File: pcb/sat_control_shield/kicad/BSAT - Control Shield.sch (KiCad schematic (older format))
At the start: 12 parts, among them P1 POWER, U1 ARDUINO_NANO_V3.0, U2 74HC4052E

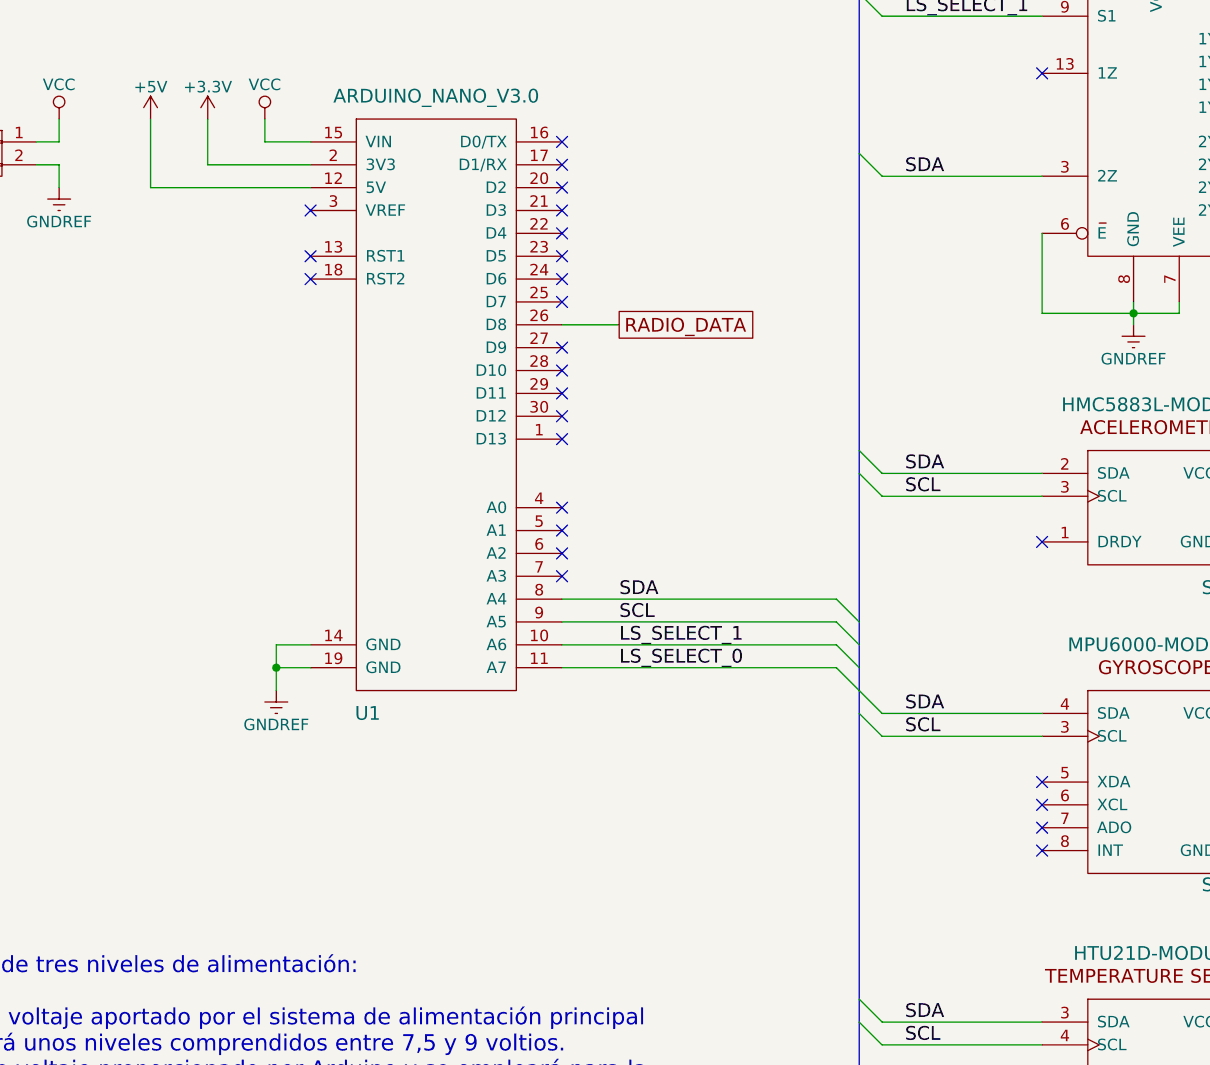
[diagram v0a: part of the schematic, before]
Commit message: refactor(control-shield): Rediseño de la placa y corrección de error en la conmutación entre sensores de intensidad luminosa.
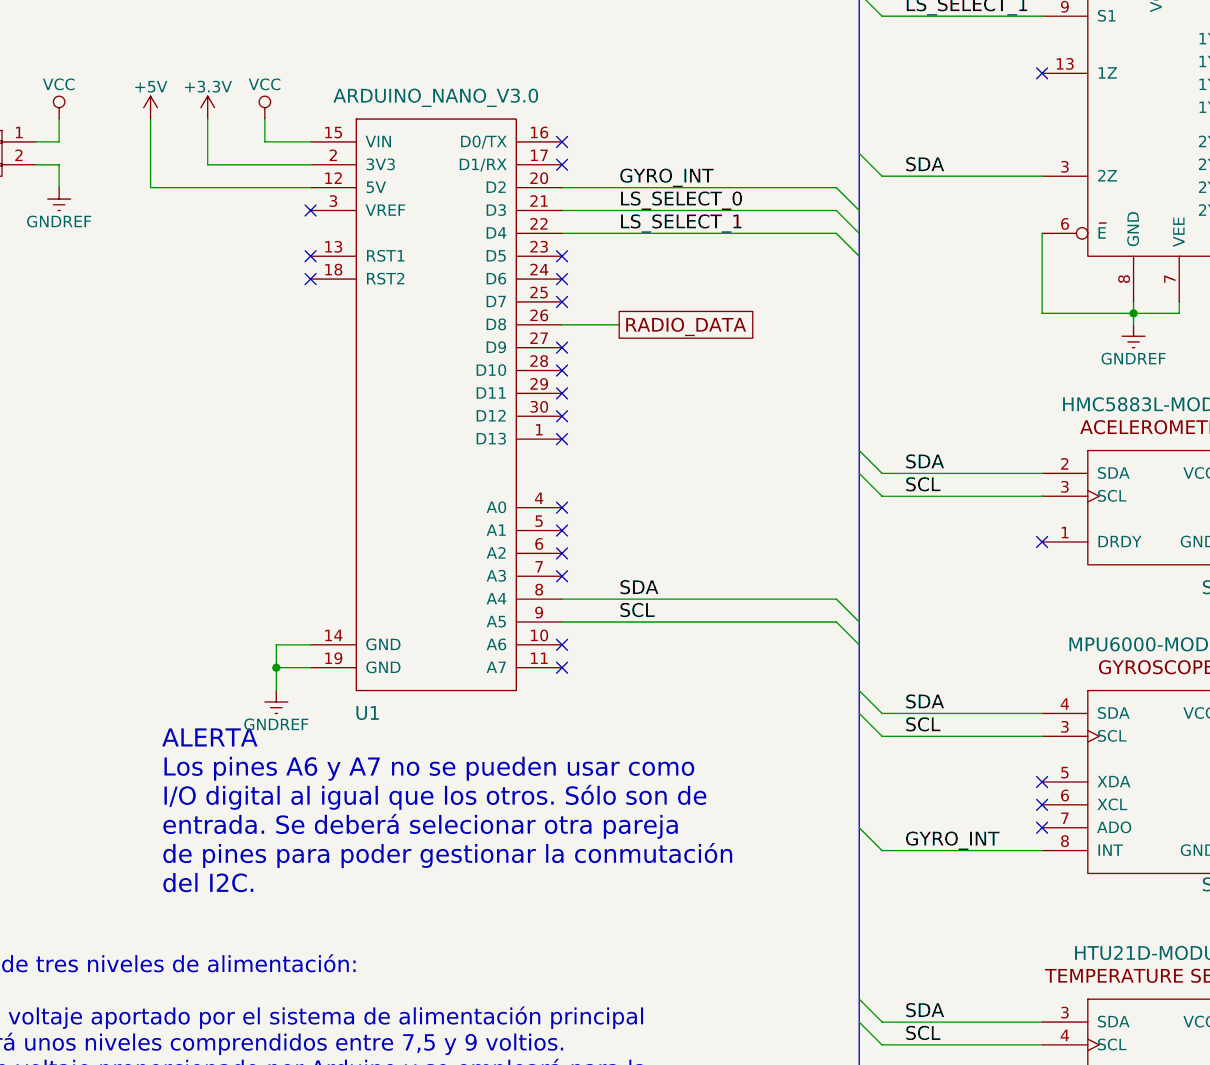
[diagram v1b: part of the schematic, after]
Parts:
- ANT1: footprint Pin_Headers:Pin_Header_Angled_1x01 -> Pin_Headers:Pin_Header_Angled_1x01_Pitch2.54mm
- P1: footprint Pin_Headers:Pin_Header_Straight_1x02 -> Pin_Headers:Pin_Header_Straight_1x02_Pitch2.54mm
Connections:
- net LS_SELECT_0: now also U1.21 (D3); no longer U1.11 (A7)
- net LS_SELECT_1: now also U1.22 (D4); no longer U1.10 (A6)
- net GYRO_INT: now reaches U1.20 (D2)
- net GYRO_INT: now also S2.8 (INT)
- no-connect marks 30 -> 28
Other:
- note added: "ALERTA\nLos pines A6 y A7 no se pueden usar como \nI/O digital al igual que los otros. Sólo son de \nentrada. Se deberá selecionar otra pareja \nde pines para poder gestionar la conmutación \ndel I2C."
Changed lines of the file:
@@
 F 0 "ANT1" H 8600 4850 60  0000 R CNN
 F 1 "ANTENNA-1" H 8600 4950 60  0000 R CNN
-F 2 "Pin_Headers:Pin_Header_Angled_1x01" H 8650 5000 60  0001 C CNN
+F 2 "Pin_Headers:Pin_Header_Angled_1x01_Pitch2.54mm" H 8650 5000 60  0001 C CNN
 F 3 "" H 8650 5000 60  0000 C CNN
 	1    8650 5000
@@
 F 0 "P1" H 1600 2300 50  0000 C CNN
 F 1 "POWER" V 1700 2150 50  0000 C CNN
-F 2 "Pin_Headers:Pin_Header_Straight_1x02" H 1600 2150 50  0001 C CNN
+F 2 "Pin_Headers:Pin_Header_Straight_1x02_Pitch2.54mm" H 1600 2150 50  0001 C CNN
 F 3 "" H 1600 2150 50  0000 C CNN
 	1    1600 2150
@@
 NoConn ~ 6200 5000
 NoConn ~ 6200 5100
-NoConn ~ 6200 5200
 $Comp
 L GNDREF #PWR017
@@
 Entry Wire Line
 	5300 4200 5400 4300
-Text Label 4350 4400 0    60   ~ 0
+Text Label 4350 2400 0    60   ~ 0
 LS_SELECT_0
-Text Label 4350 4300 0    60   ~ 0
+Text Label 4350 2500 0    60   ~ 0
 LS_SELECT_1
 Text Label 5600 1550 0    60   ~ 0
@@
 NoConn ~ 4100 2700
 NoConn ~ 4100 2600
-NoConn ~ 4100 2500
 NoConn ~ 4100 2200
 NoConn ~ 4100 2100
 NoConn ~ 4100 3200
 NoConn ~ 4100 3300
-NoConn ~ 4100 2300
-NoConn ~ 4100 2400
 Wire Wire Line
 	2800 2000 2800 2100
@@
 	5400 700  8100 700
 Entry Wire Line
-	5300 4300 5400 4400
-Entry Wire Line
-	5300 4400 5400 4500
-Wire Wire Line
-	5300 4300 4100 4300
-Wire Wire Line
-	5300 4400 4100 4400
+	5300 2400 5400 2500
+Entry Wire Line
+	5300 2500 5400 2600
+Wire Wire Line
+	5300 2400 4100 2400
+Wire Wire Line
+	5300 2500 4100 2500
 NoConn ~ 4100 3900
 NoConn ~ 4100 4000
@@
 63 88 21 86 6D 23 46 24 31 C4 10 C3 B6 11 23 92 18 62 88 61 DB 88 11 49 0C 31 C4 B0 6D C4 88 24
 86 18 62 D8 36 62 44 12 43 0C 31 6C 1B 31 22 89 21 86 18 B6 8D 18 91 C4 10 43 0C DB 46 8C 48 62
-88 21 86 6D E3 FF 07 DC F5 6D 6C 7D E1 AE A5 00 00 00 00 49 45 4E 44 AE 42 60 82 00
+88 21 86 6D E3 FF 07 DC F5 6D 6C 7D E1 AE A5 00 00 00 00 49 45 4E 44 AE 42 60 82
 EndData
 $EndBitmap
@@
 Text Label 5600 6050 0    60   ~ 0
 SCL
+Entry Wire Line
+	5400 5100 5500 5200
+Wire Wire Line
+	5500 5200 6200 5200
+Text Label 5600 5200 0    60   ~ 0
+GYRO_INT
+Entry Wire Line
+	5300 2300 5400 2400
+Wire Wire Line
+	4100 2300 5300 2300
+Text Label 4350 2300 0    60   ~ 0
+GYRO_INT
+Text Notes 2350 5400 0    79   ~ 0
+ALERTA\nLos pines A6 y A7 no se pueden usar como \nI/O digital al igual que los otros. Sólo son de \nentrada. Se deberá selecionar otra pareja \nde pines para poder gestionar la conmutación \ndel I2C.
+NoConn ~ 4100 4300
+NoConn ~ 4100 4400
 $EndSCHEMATC
